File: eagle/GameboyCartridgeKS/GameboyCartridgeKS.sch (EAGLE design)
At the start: 1 part

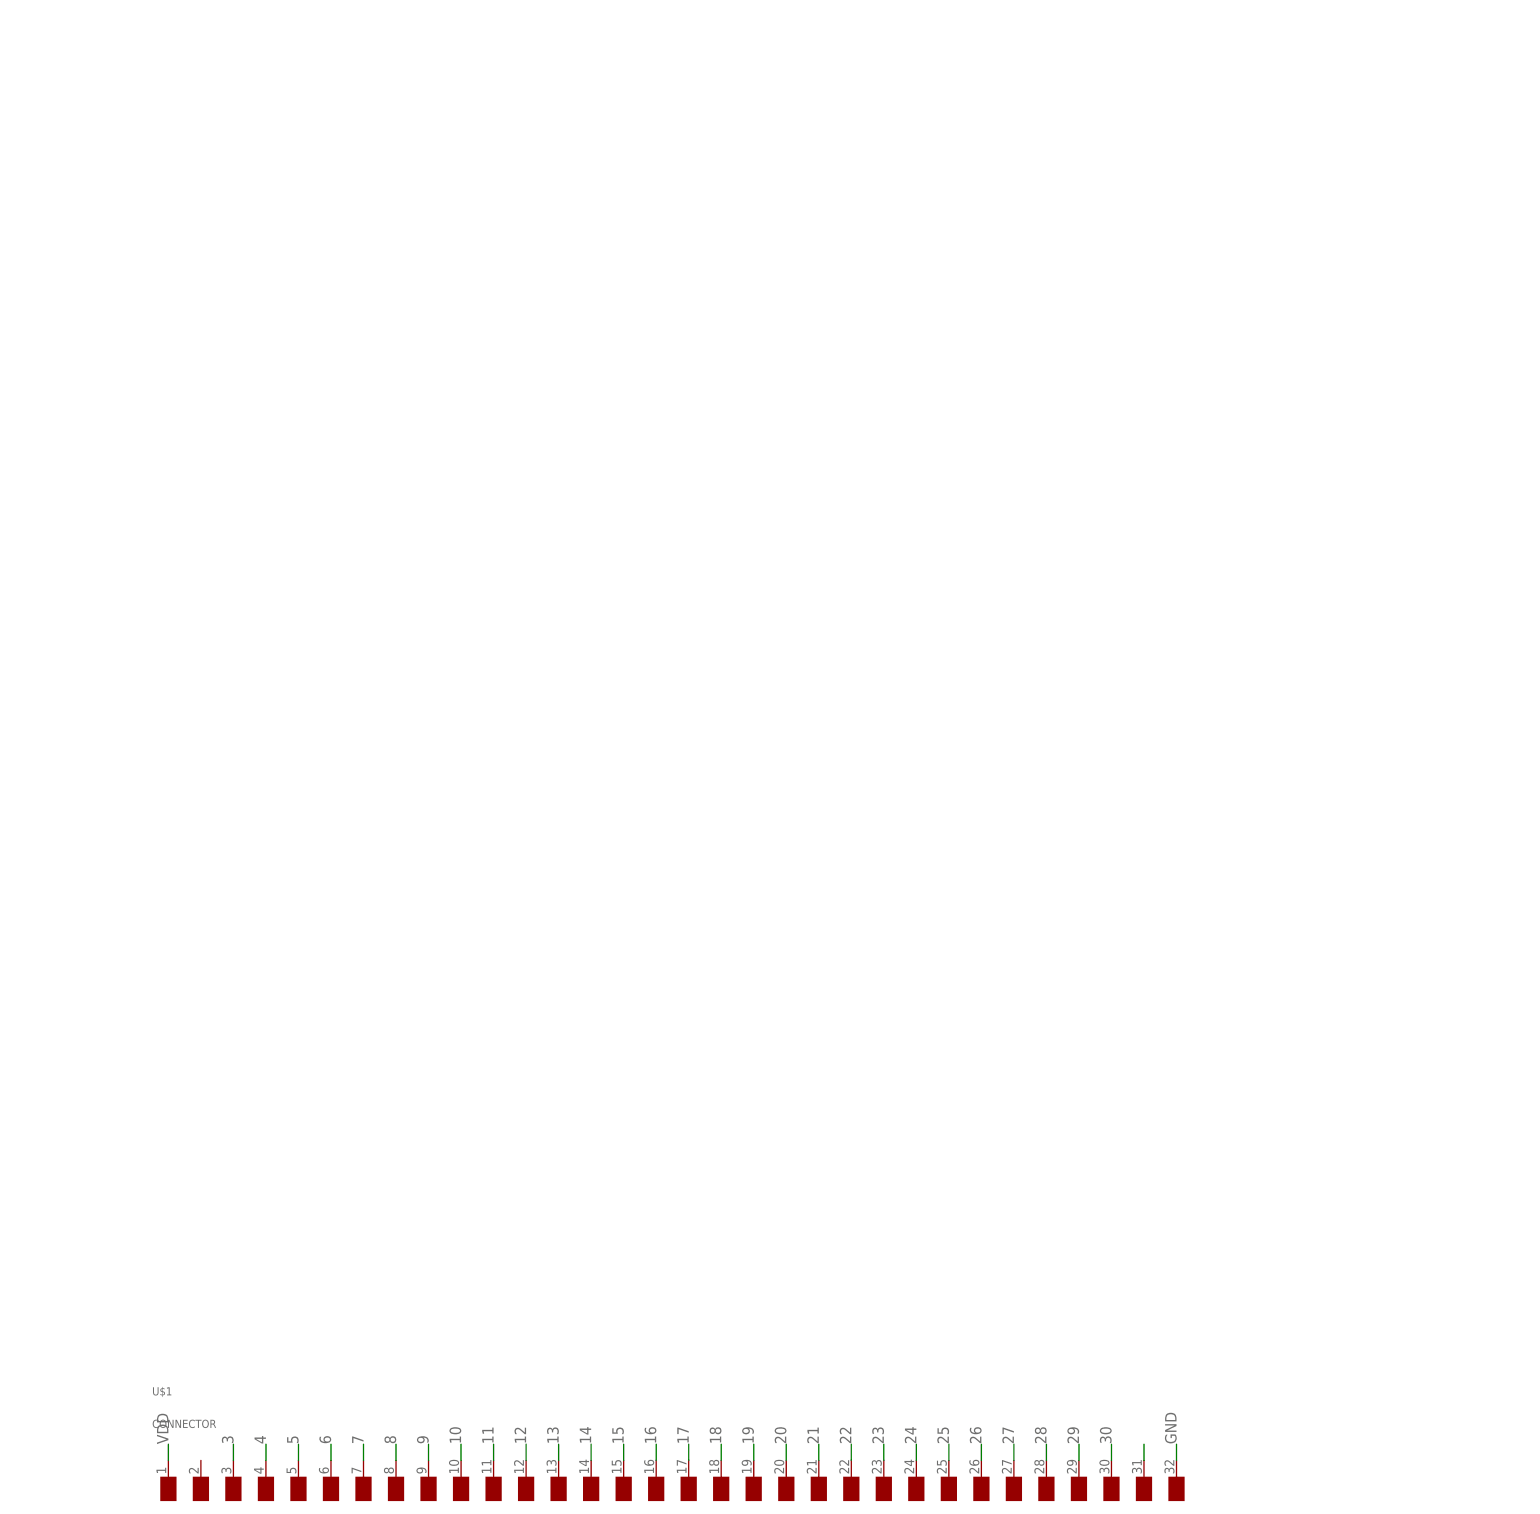
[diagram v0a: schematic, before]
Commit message: Before wiring the address bus. Replaced chip by ATmega64a.
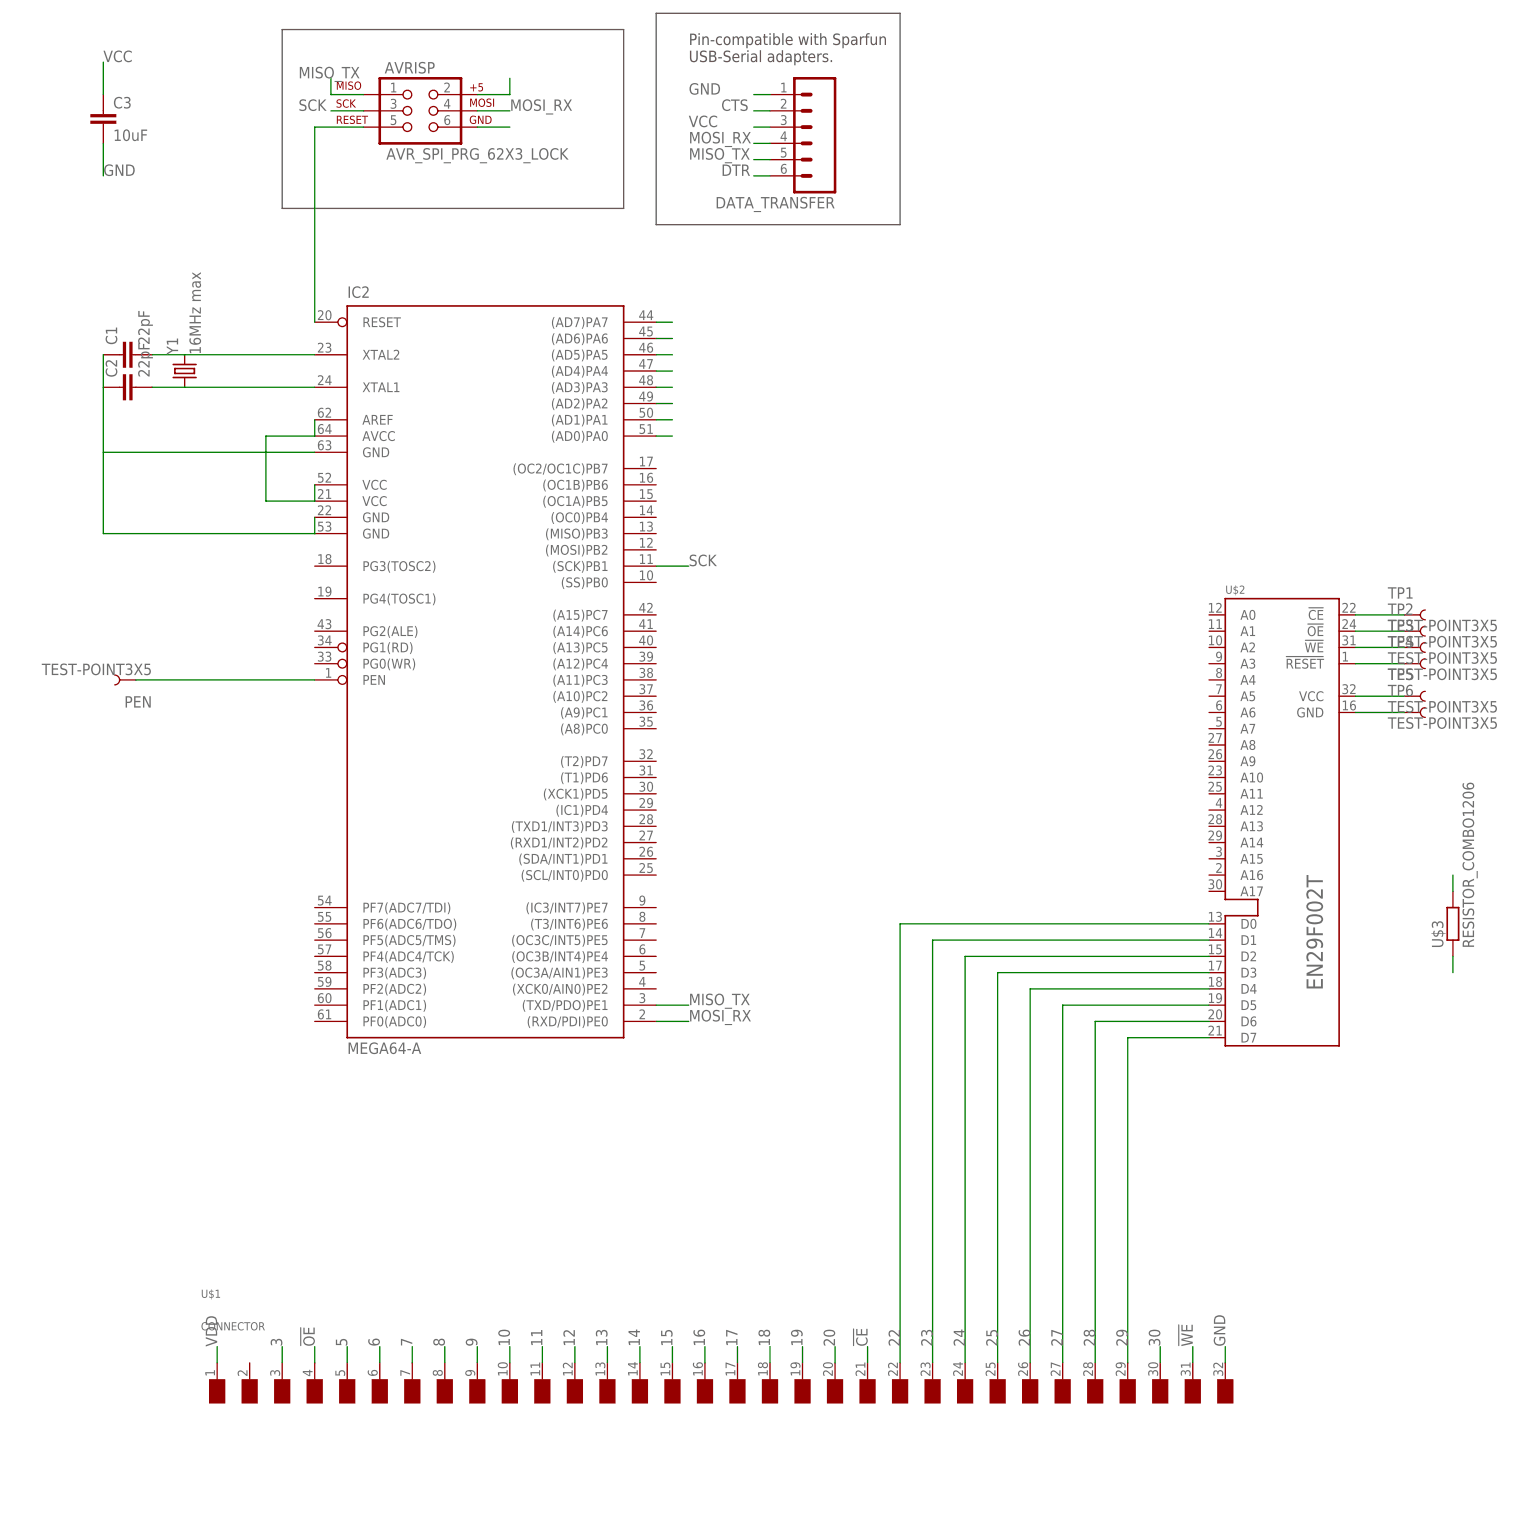
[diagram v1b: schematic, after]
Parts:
- added AVRISP: AVR_SPI_PRG_62X3_LOCK, SparkFun-Connectors:AVR_SPI_PRG_62X3_LOCK
- added C1, C2: 22pF, resistor:C-EU025-024X044
- added C3: 10uF, resistor:C-EUC1206
- added DATA_TRANSFER: (no value), SparkFun-Connectors:M06SILK_FEMALE_PTH
- added IC2: MEGA64-A, atmel:MEGA64-A
- added PEN, TP1, TP2, TP3, TP4, TP5, TP6: TEST-POINT3X5, SparkFun-Passives:TEST-POINT3X5
- added U$2: EN29F002T, kalshagar:EN29F002T
- added U$3: RESISTOR_COMBO1206, kalshagar:RESISTOR_COMBO1206
- added Y1: 16MHz max, SparkFun-FreqCtrl:CRYSTALHC49UV
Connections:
- removed net 21: U$1.A15
- removed net 31: U$1.VIN
- removed net 4: U$1./RD
- new net !CE: TP1.1, U$1.A15, U$2.!CE
- new net !OE: TP2.1, U$1./RD, U$2.!OE
- new net !RESET: TP4.1, U$2.!RESET
- new net !WE: TP3.1, U$1.VIN, U$2.!WE, U$3.1
- new net CTS: DATA_TRANSFER.2
- new net DTR: DATA_TRANSFER.6
- new net MISO_TX: AVRISP.1, DATA_TRANSFER.5, IC2.(TXD/PDO)PE1
- new net MOSI_RX: AVRISP.4, DATA_TRANSFER.4, IC2.(RXD/PDI)PE0
- new net N$2: C1.2, IC2.XTAL2, Y1.2
- new net N$3: AVRISP.5, IC2.RESET
- new net N$4: C2.2, IC2.XTAL1, Y1.1
- new net PEN: IC2.PEN, PEN.1
- new net SCK: AVRISP.3, IC2.(SCK)PB1
- new net VCC: AVRISP.2, C3.1, DATA_TRANSFER.3, IC2.AREF, IC2.AVCC, IC2.VCC, IC2.VCC@1, TP5.1, U$2.VCC, U$3.2
- net 22: now also IC2.(AD0)PA0, U$2.D0
- net 23: now also IC2.(AD1)PA1, U$2.D1
- net 24: now also IC2.(AD2)PA2, U$2.D2
- net 25: now also IC2.(AD3)PA3, U$2.D3
- net 26: now also IC2.(AD4)PA4, U$2.D4
- net 27: now also IC2.(AD5)PA5, U$2.D5
- net 28: now also IC2.(AD6)PA6, U$2.D6
- net 29: now also IC2.(AD7)PA7, U$2.D7
- net GND: now also AVRISP.6, C1.1, C2.1, C3.2, DATA_TRANSFER.1, IC2.GND, IC2.GND@1, IC2.GND@2, TP6.1, U$2.GND
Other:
- note added: "Pin-compatible with Sparfun USB-Serial adapters."
- moved on the sheet: U$1

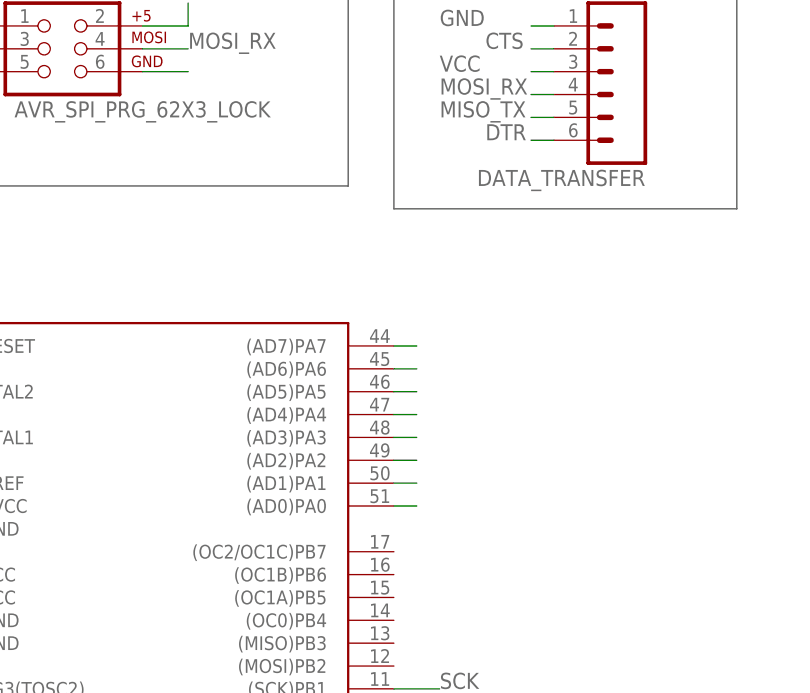
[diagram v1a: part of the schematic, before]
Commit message: Stopped in the middle of wiring, will first make a modest version with simply a eeprom programmer.
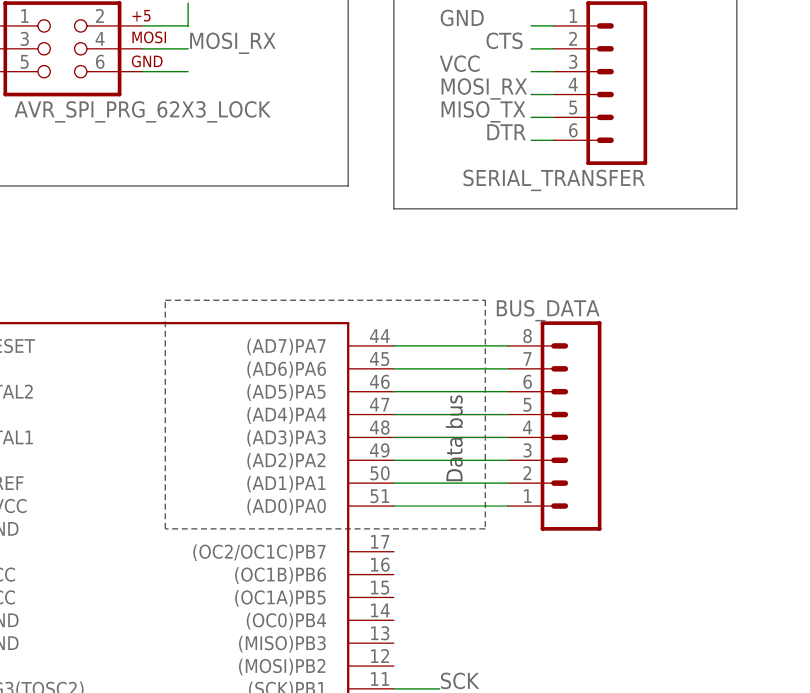
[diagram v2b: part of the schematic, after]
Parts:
- added BUS_DATA: (no value), SparkFun-Connectors:M08NO_SILK
- C1, C2: device resistor:C-EU025-024X044 -> resistor:C-EUC0805K
- C3: device resistor:C-EUC1206 -> resistor:C-EUC1206K
- renumbered DATA_TRANSFER to SERIAL_TRANSFER
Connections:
- net 22: now also BUS_DATA.1
- net 23: now also BUS_DATA.2
- net 24: now also BUS_DATA.3
- net 25: now also BUS_DATA.4
- net 26: now also BUS_DATA.5
- net 27: now also BUS_DATA.6
- net 28: now also BUS_DATA.7
- net 29: now also BUS_DATA.8
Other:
- note added: "Data bus"
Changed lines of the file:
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@@
 <part name="U$2" library="kalshagar" deviceset="EN29F002T" device=""/>
 <part name="AVRISP" library="SparkFun-Connectors" deviceset="AVR_SPI_PRG_6" device="2X3_LOCK"/>
-<part name="DATA_TRANSFER" library="SparkFun-Connectors" deviceset="M06" device="SILK_FEMALE_PTH"/>
+<part name="SERIAL_TRANSFER" library="SparkFun-Connectors" deviceset="M06" device="SILK_FEMALE_PTH"/>
 <part name="TP1" library="SparkFun-Passives" deviceset="TEST-POINT" device="3X5"/>
 <part name="TP2" library="SparkFun-Passives" deviceset="TEST-POINT" device="3X5"/>
@@
 <part name="TP6" library="SparkFun-Passives" deviceset="TEST-POINT" device="3X5"/>
 <part name="Y1" library="SparkFun-FreqCtrl" deviceset="CRYSTAL" device="HC49UV" value="16MHz max"/>
-<part name="C1" library="resistor" deviceset="C-EU" device="025-024X044" value="22pF"/>
-<part name="C2" library="resistor" deviceset="C-EU" device="025-024X044" value="22pF"/>
+<part name="C1" library="resistor" deviceset="C-EU" device="C0805K" value="22pF"/>
+<part name="C2" library="resistor" deviceset="C-EU" device="C0805K" value="22pF"/>
 <part name="U$3" library="kalshagar" deviceset="RESISTOR_COMBO1206" device=""/>
 <part name="IC2" library="atmel" deviceset="MEGA64" device="-A"/>
 <part name="PEN" library="SparkFun-Passives" deviceset="TEST-POINT" device="3X5"/>
-<part name="C3" library="resistor" deviceset="C-EU" device="C1206" value="10uF"/>
+<part name="C3" library="resistor" deviceset="C-EU" device="C1206K" value="10uF"/>
+<part name="BUS_DATA" library="SparkFun-Connectors" deviceset="M08" device="NO_SILK"/>
 </parts>
 <sheets>
@@
 <wire x1="63.5" y1="248.92" x2="10.16" y2="248.92" width="0.1524" layer="97"/>
 <wire x1="10.16" y1="248.92" x2="10.16" y2="276.86" width="0.1524" layer="97"/>
+<wire x1="43.18" y1="236.22" x2="78.74" y2="236.22" width="0.1524" layer="97" style="shortdash"/>
+<wire x1="78.74" y1="236.22" x2="78.74" y2="210.82" width="0.1524" layer="97" style="shortdash"/>
+<wire x1="78.74" y1="210.82" x2="43.18" y2="210.82" width="0.1524" layer="97" style="shortdash"/>
+<wire x1="43.18" y1="210.82" x2="43.18" y2="236.22" width="0.1524" layer="97" style="shortdash"/>
+<text x="76.2" y="215.9" size="1.778" layer="97" rot="R90">Data bus</text>
 </plain>
 <instances>
@@
 <instance part="U$2" gate="G$1" x="172.72" y="160.02"/>
 <instance part="AVRISP" gate="G$1" x="30.48" y="264.16"/>
-<instance part="DATA_TRANSFER" gate="G$1" x="91.44" y="261.62" rot="R180"/>
+<instance part="SERIAL_TRANSFER" gate="G$1" x="91.44" y="261.62" rot="R180"/>
 <instance part="TP1" gate="G$1" x="185.42" y="185.42"/>
 <instance part="TP2" gate="G$1" x="185.42" y="182.88"/>
@@
 <instance part="PEN" gate="G$1" x="-12.7" y="175.26" rot="R180"/>
 <instance part="C3" gate="G$1" x="-17.78" y="264.16"/>
+<instance part="BUS_DATA" gate="G$1" x="86.36" y="220.98" rot="MR0"/>
 </instances>
 <busses>
@@
 <segment>
 <pinref part="IC2" gate="G$1" pin="(AD0)PA0"/>
-<wire x1="68.58" y1="213.36" x2="71.12" y2="213.36" width="0.1524" layer="91"/>
+<wire x1="68.58" y1="213.36" x2="81.28" y2="213.36" width="0.1524" layer="91"/>
+<pinref part="BUS_DATA" gate="G$1" pin="1"/>
 </segment>
 </net>
@@
 <segment>
 <pinref part="IC2" gate="G$1" pin="(AD1)PA1"/>
-<wire x1="68.58" y1="215.9" x2="71.12" y2="215.9" width="0.1524" layer="91"/>
+<wire x1="68.58" y1="215.9" x2="81.28" y2="215.9" width="0.1524" layer="91"/>
+<pinref part="BUS_DATA" gate="G$1" pin="2"/>
 </segment>
 </net>
@@
 <segment>
 <pinref part="IC2" gate="G$1" pin="(AD2)PA2"/>
-<wire x1="68.58" y1="218.44" x2="71.12" y2="218.44" width="0.1524" layer="91"/>
+<wire x1="68.58" y1="218.44" x2="81.28" y2="218.44" width="0.1524" layer="91"/>
+<pinref part="BUS_DATA" gate="G$1" pin="3"/>
 </segment>
 </net>
@@
 <segment>
 <pinref part="IC2" gate="G$1" pin="(AD3)PA3"/>
-<wire x1="68.58" y1="220.98" x2="71.12" y2="220.98" width="0.1524" layer="91"/>
+<wire x1="68.58" y1="220.98" x2="81.28" y2="220.98" width="0.1524" layer="91"/>
+<pinref part="BUS_DATA" gate="G$1" pin="4"/>
 </segment>
 </net>
@@
 <segment>
 <pinref part="IC2" gate="G$1" pin="(AD4)PA4"/>
-<wire x1="68.58" y1="223.52" x2="71.12" y2="223.52" width="0.1524" layer="91"/>
+<wire x1="68.58" y1="223.52" x2="81.28" y2="223.52" width="0.1524" layer="91"/>
+<pinref part="BUS_DATA" gate="G$1" pin="5"/>
 </segment>
 </net>
@@
 </segment>
 <segment>
-<pinref part="DATA_TRANSFER" gate="G$1" pin="1"/>
+<pinref part="SERIAL_TRANSFER" gate="G$1" pin="1"/>
 <wire x1="86.36" y1="266.7" x2="83.82" y2="266.7" width="0.1524" layer="91"/>
 <label x="73.66" y="266.7" size="1.778" layer="95"/>
@@
 <segment>
 <pinref part="IC2" gate="G$1" pin="(AD5)PA5"/>
-<wire x1="68.58" y1="226.06" x2="71.12" y2="226.06" width="0.1524" layer="91"/>
+<wire x1="68.58" y1="226.06" x2="81.28" y2="226.06" width="0.1524" layer="91"/>
+<pinref part="BUS_DATA" gate="G$1" pin="6"/>
 </segment>
 </net>
@@
 <segment>
 <pinref part="IC2" gate="G$1" pin="(AD6)PA6"/>
-<wire x1="68.58" y1="228.6" x2="71.12" y2="228.6" width="0.1524" layer="91"/>
+<wire x1="68.58" y1="228.6" x2="81.28" y2="228.6" width="0.1524" layer="91"/>
+<pinref part="BUS_DATA" gate="G$1" pin="7"/>
 </segment>
 </net>
@@
 <segment>
 <pinref part="IC2" gate="G$1" pin="(AD7)PA7"/>
-<wire x1="68.58" y1="231.14" x2="71.12" y2="231.14" width="0.1524" layer="91"/>
+<wire x1="68.58" y1="231.14" x2="81.28" y2="231.14" width="0.1524" layer="91"/>
+<pinref part="BUS_DATA" gate="G$1" pin="8"/>
 </segment>
 </net>
@@
 </segment>
 <segment>
-<pinref part="DATA_TRANSFER" gate="G$1" pin="3"/>
+<pinref part="SERIAL_TRANSFER" gate="G$1" pin="3"/>
 <wire x1="86.36" y1="261.62" x2="83.82" y2="261.62" width="0.1524" layer="91"/>
 <label x="73.66" y="261.62" size="1.778" layer="95"/>
@@
 </segment>
 <segment>
-<pinref part="DATA_TRANSFER" gate="G$1" pin="5"/>
+<pinref part="SERIAL_TRANSFER" gate="G$1" pin="5"/>
 <wire x1="86.36" y1="256.54" x2="83.82" y2="256.54" width="0.1524" layer="91"/>
 <label x="73.66" y="256.54" size="1.778" layer="95"/>
@@
 </segment>
 <segment>
-<pinref part="DATA_TRANSFER" gate="G$1" pin="4"/>
+<pinref part="SERIAL_TRANSFER" gate="G$1" pin="4"/>
 <wire x1="86.36" y1="259.08" x2="83.82" y2="259.08" width="0.1524" layer="91"/>
 <label x="73.66" y="259.08" size="1.778" layer="95"/>
@@
 <net name="CTS" class="0">
 <segment>
-<pinref part="DATA_TRANSFER" gate="G$1" pin="2"/>
+<pinref part="SERIAL_TRANSFER" gate="G$1" pin="2"/>
 <wire x1="86.36" y1="264.16" x2="83.82" y2="264.16" width="0.1524" layer="91"/>
 <label x="78.74" y="264.16" size="1.778" layer="95"/>
@@
 <net name="DTR" class="0">
 <segment>
-<pinref part="DATA_TRANSFER" gate="G$1" pin="6"/>
+<pinref part="SERIAL_TRANSFER" gate="G$1" pin="6"/>
 <wire x1="86.36" y1="254" x2="83.82" y2="254" width="0.1524" layer="91"/>
 <label x="78.74" y="254" size="1.778" layer="95"/>
